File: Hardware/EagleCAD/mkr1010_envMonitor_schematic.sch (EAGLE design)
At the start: 6 parts, among them J1 SGP30, J2 PMSA003I, J3 MEMS MIC, J4 TEST_POINTS, J5 RESET, U1 ARDUINO_MKR_ZERO

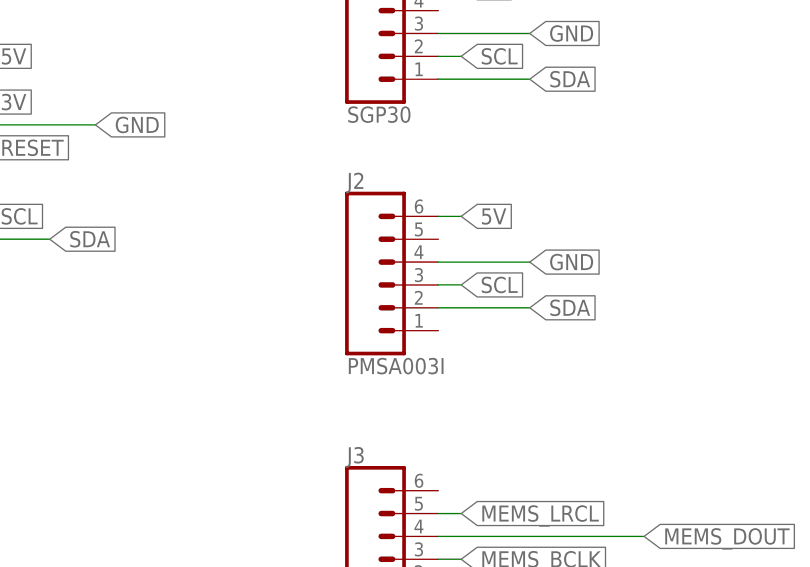
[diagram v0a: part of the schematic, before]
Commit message: Corrected PMSA003I board layout (6pin vs 7pin header)
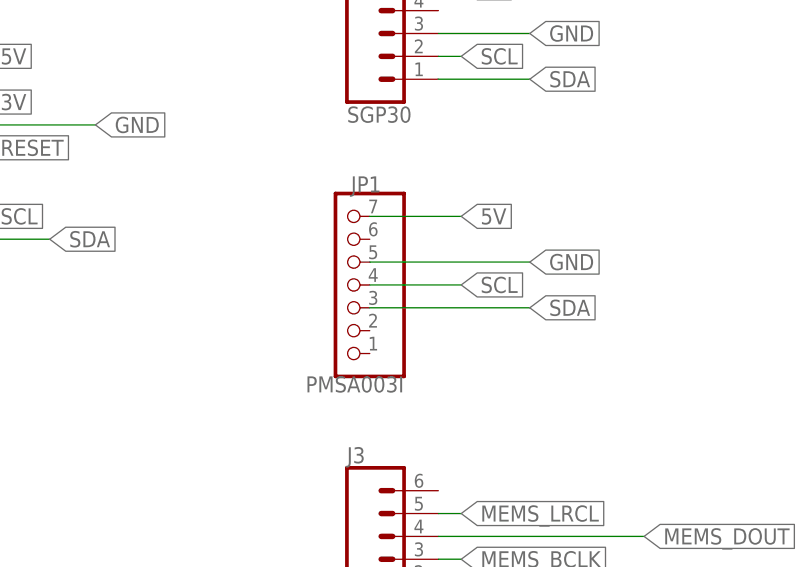
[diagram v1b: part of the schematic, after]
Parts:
- removed J2: PMSA003I, SparkFun-Connectors:CONN_06NO_SILK_FEMALE_PTH
- added JP1: PMSA003I, pinhead:PINHD-1X7
- J3: device SparkFun-Connectors:CONN_06NO_SILK_FEMALE_PTH -> SparkFun-Connectors:CONN_06SILK_FEMALE_PTH
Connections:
- net 5V: now also JP1.7; no longer J2.6
- net GND: now also JP1.5; no longer J2.4
- net SCL: now also JP1.4; no longer J2.3
- net SDA: now also JP1.3; no longer J2.2
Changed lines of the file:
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@@
 <part name="U1" library="ARDUINO_MKR_ZERO" deviceset="ARDUINO_MKR_ZERO" device=""/>
 <part name="J1" library="SparkFun-Connectors" library_urn="urn:adsk.eagle:library:513" deviceset="CONN_05" device="" package3d_urn="urn:adsk.eagle:package:38104/1" value="SGP30"/>
-<part name="J2" library="SparkFun-Connectors" library_urn="urn:adsk.eagle:library:513" deviceset="CONN_06" device="NO_SILK_FEMALE_PTH" package3d_urn="urn:adsk.eagle:package:38130/1" value="PMSA003I"/>
-<part name="J3" library="SparkFun-Connectors" library_urn="urn:adsk.eagle:library:513" deviceset="CONN_06" device="NO_SILK_FEMALE_PTH" package3d_urn="urn:adsk.eagle:package:38130/1" value="MEMS MIC"/>
+<part name="J3" library="SparkFun-Connectors" library_urn="urn:adsk.eagle:library:513" deviceset="CONN_06" device="SILK_FEMALE_PTH" package3d_urn="urn:adsk.eagle:package:38009/1" value="MEMS MIC"/>
 <part name="J4" library="SparkFun-Connectors" library_urn="urn:adsk.eagle:library:513" deviceset="CONN_05" device="" package3d_urn="urn:adsk.eagle:package:38104/1" value="TEST_POINTS"/>
 <part name="J5" library="SparkFun-Connectors" library_urn="urn:adsk.eagle:library:513" deviceset="CONN_02" device="" package3d_urn="urn:adsk.eagle:package:38039/1" value="RESET"/>
+<part name="JP1" library="pinhead" library_urn="urn:adsk.eagle:library:325" deviceset="PINHD-1X7" device="" package3d_urn="urn:adsk.eagle:package:22477/2" value="PMSA003I"/>
 </parts>
 <sheets>
@@
 <attribute name="NAME" x="132.08" y="91.948" size="1.778" layer="95" font="vector"/>
 </instance>
-<instance part="J2" gate="G$1" x="137.16" y="55.88" smashed="yes">
-<attribute name="VALUE" x="132.08" y="45.974" size="1.778" layer="96" font="vector"/>
-<attribute name="NAME" x="132.08" y="66.548" size="1.778" layer="95" font="vector"/>
-</instance>
 <instance part="J3" gate="G$1" x="137.16" y="25.4" smashed="yes">
 <attribute name="VALUE" x="132.08" y="15.494" size="1.778" layer="96" font="vector"/>
@@
 <attribute name="VALUE" x="20.32" y="15.494" size="1.778" layer="96" font="vector"/>
 <attribute name="NAME" x="20.32" y="25.908" size="1.778" layer="95" font="vector"/>
+</instance>
+<instance part="JP1" gate="A" x="132.08" y="55.88" smashed="yes" rot="R180">
+<attribute name="NAME" x="135.89" y="67.945" size="1.778" layer="95" rot="R180"/>
+<attribute name="VALUE" x="138.43" y="45.72" size="1.778" layer="96" rot="R180"/>
 </instance>
 </instances>
@@
 </segment>
 <segment>
-<pinref part="J2" gate="G$1" pin="4"/>
-<wire x1="142.24" y1="58.42" x2="152.4" y2="58.42" width="0.1524" layer="91"/>
+<wire x1="134.62" y1="58.42" x2="152.4" y2="58.42" width="0.1524" layer="91"/>
 <label x="152.4" y="58.42" size="1.778" layer="95" xref="yes"/>
+<pinref part="JP1" gate="A" pin="5"/>
 </segment>
 <segment>
@@
 </segment>
 <segment>
-<pinref part="J2" gate="G$1" pin="6"/>
-<wire x1="142.24" y1="63.5" x2="144.78" y2="63.5" width="0.1524" layer="91"/>
 <label x="144.78" y="63.5" size="1.778" layer="95" xref="yes"/>
+<pinref part="JP1" gate="A" pin="7"/>
+<wire x1="144.78" y1="63.5" x2="134.62" y2="63.5" width="0.1524" layer="91"/>
 </segment>
 <segment>
@@
 </segment>
 <segment>
-<pinref part="J2" gate="G$1" pin="3"/>
-<wire x1="142.24" y1="55.88" x2="144.78" y2="55.88" width="0.1524" layer="91"/>
 <label x="144.78" y="55.88" size="1.778" layer="95" xref="yes"/>
+<pinref part="JP1" gate="A" pin="4"/>
+<wire x1="144.78" y1="55.88" x2="134.62" y2="55.88" width="0.1524" layer="91"/>
 </segment>
 <segment>
@@
 </segment>
 <segment>
-<pinref part="J2" gate="G$1" pin="2"/>
-<wire x1="142.24" y1="53.34" x2="152.4" y2="53.34" width="0.1524" layer="91"/>
+<wire x1="134.62" y1="53.34" x2="152.4" y2="53.34" width="0.1524" layer="91"/>
 <label x="152.4" y="53.34" size="1.778" layer="95" xref="yes"/>
+<pinref part="JP1" gate="A" pin="3"/>
 </segment>
 <segment>
